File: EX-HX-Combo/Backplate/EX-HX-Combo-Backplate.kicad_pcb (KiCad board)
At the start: 2 copper layers, 17.5 x 120.2 mm, 8 parts

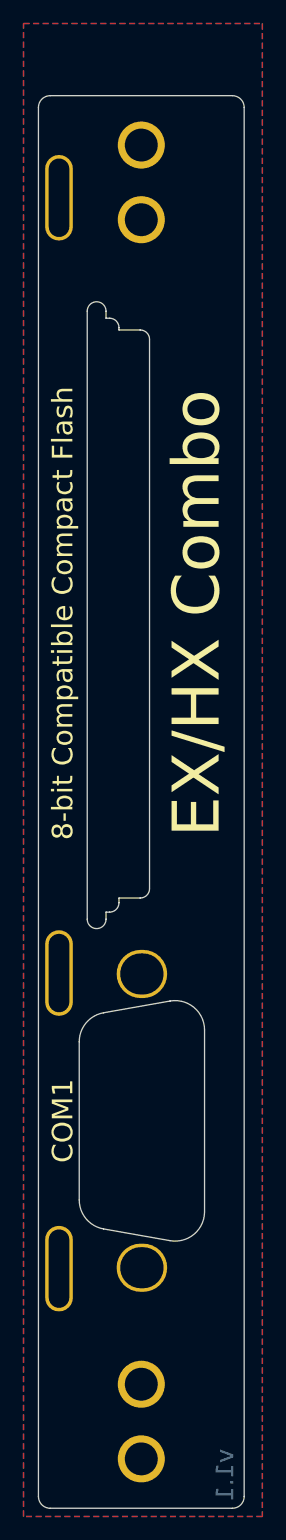
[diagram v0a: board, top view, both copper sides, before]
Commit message: EX-HX-Combo: Relocate back plate alignment tabs to very ends of boards. Also make them 1mm narrower. Remove middle alighment tab.
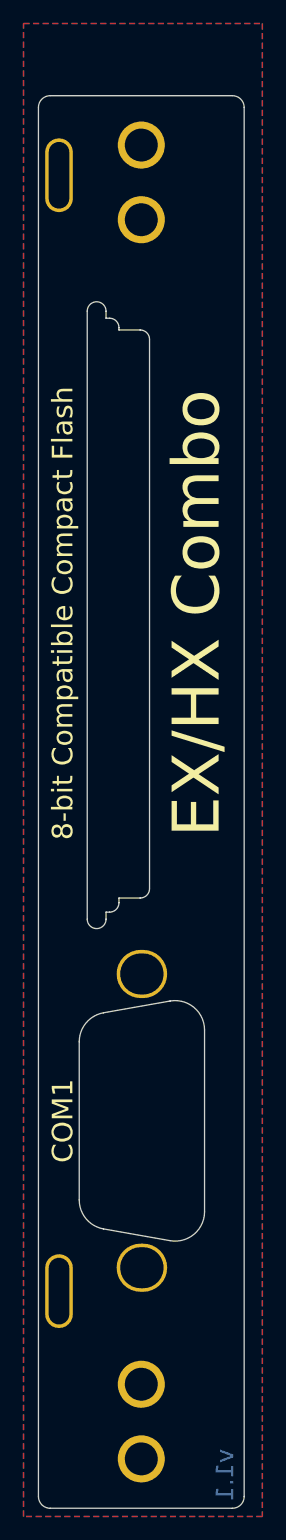
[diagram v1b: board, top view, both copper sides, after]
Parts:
- removed the H7 at (254.5, 41.5)
- moved H6 67.9 mm to (254.5, 39.6)
- moved H5 1.91 mm to (254.5, 134.5)
- renumbered H8 to H7

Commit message: Update boards.
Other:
- board text added: "Created by Jayeson Lee-Steere https://github.com/JayesonLS/ISA-Cards"
- board text removed: "Copyright (C) 2021 Titanium Studios Pty Ltd Creative Commons Attribution-ShareAlike 4.0 International https://github.com/JayesonLS/ISA-Cards"
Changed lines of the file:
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@@
     (37 F.SilkS user)
     (38 B.Mask user)
-    (39 F.Mask user)
+    (39 F.Mask user hide)
     (40 Dwgs.User user)
     (41 Cmts.User user)
@@
       (effects (font (size 1 1) (thickness 0.15)))
     )
+    (fp_line (start -15.875 0) (end -15.875 -12.7) (layer F.CrtYd) (width 0.05))
+    (fp_line (start -15.875 -12.7) (end 15.875 -12.7) (layer F.CrtYd) (width 0.05))
+    (fp_line (start 15.875 -12.7) (end 15.875 0) (layer F.CrtYd) (width 0.05))
+    (fp_line (start 15.875 0) (end -15.875 0) (layer F.CrtYd) (width 0.05))
+    (fp_line (start -15.875 0) (end -15.875 -12.7) (layer B.CrtYd) (width 0.05))
+    (fp_line (start -15.875 -12.7) (end 15.875 -12.7) (layer B.CrtYd) (width 0.05))
+    (fp_line (start 15.875 -12.7) (end 15.875 0) (layer B.CrtYd) (width 0.05))
+    (fp_line (start 15.875 0) (end -15.875 0) (layer B.CrtYd) (width 0.05))
+    (fp_line (start 6.73 -3.42) (end 6.23 -3.92) (layer Dwgs.User) (width 0.12))
+    (fp_line (start 7.73 -9.08) (end 7.23 -8.58) (layer Dwgs.User) (width 0.12))
+    (fp_line (start 6.73 -0.92) (end 6.73 -0.42) (layer Dwgs.User) (width 0.12))
+    (fp_line (start 7.73 -11.58) (end 7.73 -12.08) (layer Dwgs.User) (width 0.12))
+    (fp_line (start -7.73 -11.58) (end -7.73 -12.08) (layer Dwgs.User) (width 0.12))
+    (fp_line (start -7.73 -9.08) (end -7.23 -8.58) (layer Dwgs.User) (width 0.12))
+    (fp_line (start -6.73 -3.42) (end -6.23 -3.92) (layer Dwgs.User) (width 0.12))
+    (fp_line (start -6.73 -0.92) (end -6.73 -0.42) (layer Dwgs.User) (width 0.12))
+    (fp_line (start 9.19197 -2.98504) (end 9.68617 -2.89804) (layer Dwgs.User) (width 0.12))
+    (fp_line (start 10.19197 -8.64504) (end 10.68617 -8.55804) (layer Dwgs.User) (width 0.12))
+    (fp_line (start -10.19197 -8.64504) (end -10.68617 -8.55804) (layer Dwgs.User) (width 0.12))
     (fp_line (start -9.19197 -2.98504) (end -9.68617 -2.89804) (layer Dwgs.User) (width 0.12))
-    (fp_line (start -10.19197 -8.64504) (end -10.68617 -8.55804) (layer Dwgs.User) (width 0.12))
-    (fp_line (start 10.19197 -8.64504) (end 10.68617 -8.55804) (layer Dwgs.User) (width 0.12))
-    (fp_line (start 9.19197 -2.98504) (end 9.68617 -2.89804) (layer Dwgs.User) (width 0.12))
-    (fp_line (start -6.73 -0.92) (end -6.73 -0.42) (layer Dwgs.User) (width 0.12))
-    (fp_line (start -6.73 -3.42) (end -6.23 -3.92) (layer Dwgs.User) (width 0.12))
-    (fp_line (start -7.73 -9.08) (end -7.23 -8.58) (layer Dwgs.User) (width 0.12))
-    (fp_line (start -7.73 -11.58) (end -7.73 -12.08) (layer Dwgs.User) (width 0.12))
-    (fp_line (start 7.73 -11.58) (end 7.73 -12.08) (layer Dwgs.User) (width 0.12))
-    (fp_line (start 6.73 -0.92) (end 6.73 -0.42) (layer Dwgs.User) (width 0.12))
-    (fp_line (start 7.73 -9.08) (end 7.23 -8.58) (layer Dwgs.User) (width 0.12))
-    (fp_line (start 6.73 -3.42) (end 6.23 -3.92) (layer Dwgs.User) (width 0.12))
-    (fp_line (start 15.875 0) (end -15.875 0) (layer B.CrtYd) (width 0.05))
-    (fp_line (start 15.875 -12.7) (end 15.875 0) (layer B.CrtYd) (width 0.05))
-    (fp_line (start -15.875 -12.7) (end 15.875 -12.7) (layer B.CrtYd) (width 0.05))
-    (fp_line (start -15.875 0) (end -15.875 -12.7) (layer B.CrtYd) (width 0.05))
-    (fp_line (start 15.875 0) (end -15.875 0) (layer F.CrtYd) (width 0.05))
-    (fp_line (start 15.875 -12.7) (end 15.875 0) (layer F.CrtYd) (width 0.05))
-    (fp_line (start -15.875 -12.7) (end 15.875 -12.7) (layer F.CrtYd) (width 0.05))
-    (fp_line (start -15.875 0) (end -15.875 -12.7) (layer F.CrtYd) (width 0.05))
     (fp_text user "To make the DB-9 hole, draw quarter circles on theDwgs.User layer usng the provided guides, move them to the edge cuts layer, then join with lines on the edge cuts layer." (at 0 -17.77 90) (layer Cmts.User)
       (effects (font (size 1 1) (thickness 0.15)))
@@
   (gr_line (start 270.23 151.97) (end 270.23 33.81) (layer Edge.Cuts) (width 0.1))
   (gr_line (start 243.24 37.54) (end 120.03 37.54) (layer Eco1.User) (width 0.1))
-  (gr_text "Copyright (C) 2021 Titanium Studios Pty Ltd\nCreative Commons Attribution-ShareAlike 4.0 International\nhttps://github.com/JayesonLS/ISA-Cards" (at 265.785 76.835 90) (layer B.SilkS)
+  (gr_text "Created by Jayeson Lee-Steere\nhttps://github.com/JayesonLS/ISA-Cards" (at 265.785 76.835 90) (layer B.SilkS)
     (effects (font (size 1 1) (thickness 0.15)) (justify mirror))
   )
